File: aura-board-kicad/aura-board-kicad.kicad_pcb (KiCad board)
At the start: 2 copper layers, 76.8 x 53.3 mm, 22 parts, among them J1 Main Power, J2 PWM Outputs, J3 BB-UART0, J4 Attopilot, J5 GPS, J6 SBUS, J7 Telemetry, U1 TSR2-2450, U2 PocketBeagle, U3 Teensy-3.2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

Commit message: Add a proper 3x08 PWM block with ground pins and the power bus tied together but not connected to board power.
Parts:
- removed ? (x2): 1x08, Pin_Headers:Pin_Header_Straight_1x08_Pitch2.54mm
- J2: value PWM Outputs -> PWM; footprint Pin_Headers:Pin_Header_Straight_1x08_Pitch2.54mm -> footprint:PWM_3x08
- moved J2 17.8 mm to (92.1, 95.2), turned to 270 degrees
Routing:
- net +5VA: track 0.00 -> 17.8 mm

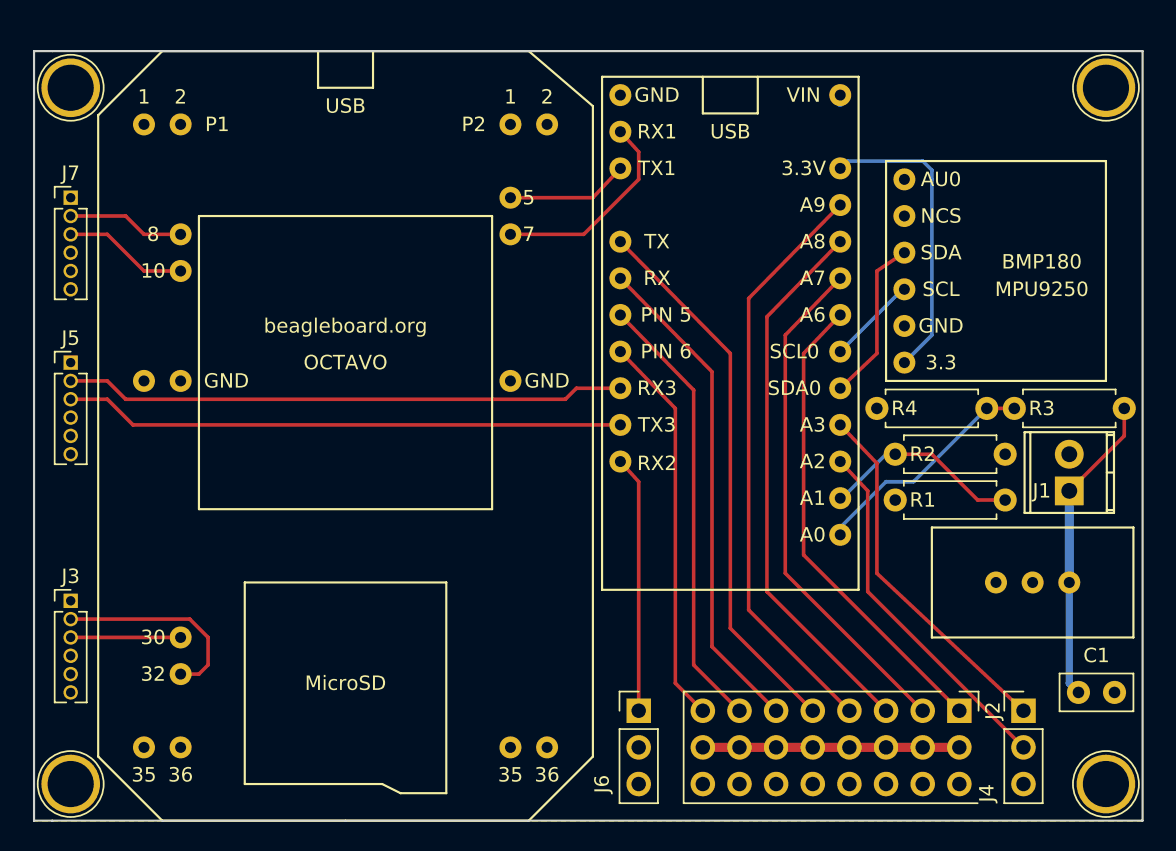
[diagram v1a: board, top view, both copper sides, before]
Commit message: Swich to picoblade 1.25mm external connectors.  DF-13 will also fit here. Pins 5 and 6 both tie to ground.  This means the assembler can pick 5 or 6 pos headers depending on their needs. This offers some flexibility to the assembler/integrator to pick the best suited connectors. Add external I2C0 connector (4-pin picoplade.)
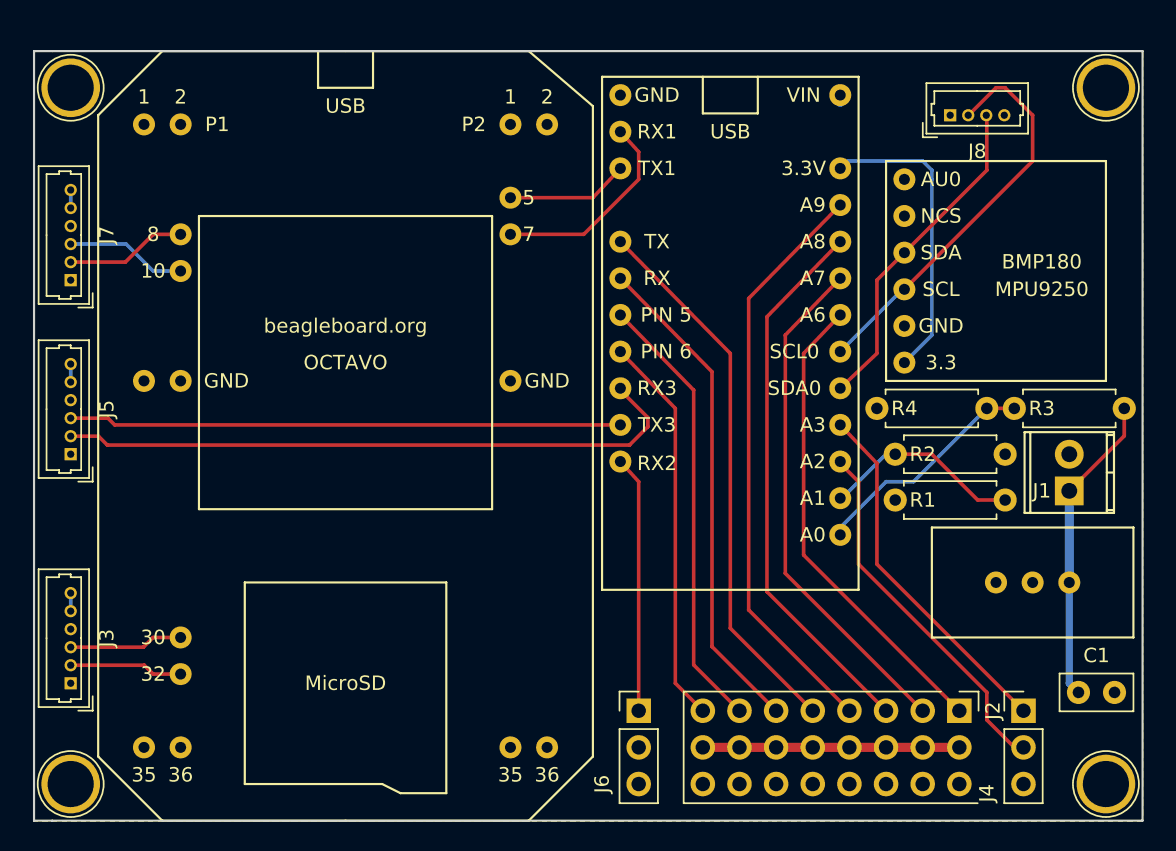
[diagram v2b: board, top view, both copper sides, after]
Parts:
- added J8: I2C0, Connectors_Molex:Molex_PicoBlade_53047-0410_04x1.25mm_Straight, F.Cu at (91.4, 54.0)
- J2: value PWM -> PWM_3x08
- J3: value BB-UART0 -> BB0; footprint Pin_Headers:Pin_Header_Straight_1x06_Pitch1.27mm -> Connectors_Molex:Molex_PicoBlade_53047-0610_06x1.25mm_Straight
- J5: footprint Pin_Headers:Pin_Header_Straight_1x06_Pitch1.27mm -> Connectors_Molex:Molex_PicoBlade_53047-0610_06x1.25mm_Straight
- J7: value Telemetry -> Tele; footprint Pin_Headers:Pin_Header_Straight_1x06_Pitch1.27mm -> Connectors_Molex:Molex_PicoBlade_53047-0610_06x1.25mm_Straight
- moved J5 6.35 mm to (30.5, 77.5), turned to 90 degrees
- moved J3 5.72 mm to (30.5, 93.3), turned to 90 degrees
- moved J7 5.72 mm to (30.5, 65.4), turned to 90 degrees
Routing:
- net /I2C0_SCL: track 6.23 -> 28.0 mm
- net /I2C0_SDA: track 11.5 -> 23.2 mm
- net /UART0_RX: track 14.1 -> 7.87 mm
- net /GPS_RX: track 38.9 -> 44.2 mm
- net GND: track 0.00 -> 3.75 mm
- net /GPS_TX: track 38.8 -> 38.3 mm
- net +5V: track 1.02 -> 0.51 mm

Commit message: Increase pad diameter (inner and outer) on all my project footprints to match standard 0.1" pin dimensions.
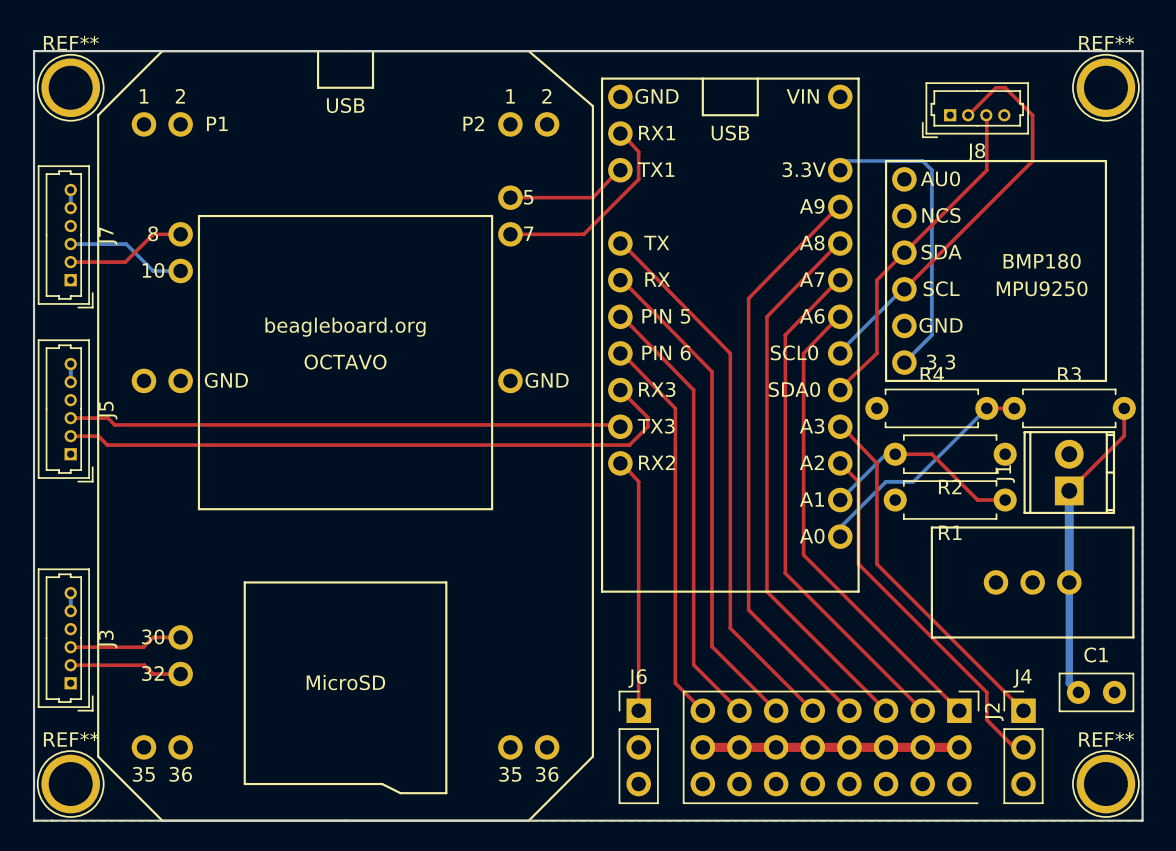
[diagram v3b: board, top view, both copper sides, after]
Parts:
- removed U1: TSR2-2450, Aura Footprints:TSR2-2450
- removed U2: PocketBeagle, Aura Footprints:PocketBeagle
- removed U3: Teensy-3.2, Aura Footprints:Teensy-3.2
- removed U4: CJMCU, Aura Footprints:CJMCU
- added THT: PocketBeagle, footprint:PocketBeagle, F.Cu at (49.5, 49.5)
- added THT: Teensy-3.2 (AuraUAS), footprint:Teensy-3.2, F.Cu at (76.2, 51.4)
- added THT: CJMCU, footprint:CJMCU, F.Cu at (94.6, 72.4)
- added THT: TSR2-2450, footprint:TSR2-2450, F.Cu at (97.2, 90.2)
- J3: value BB0 -> BBCON
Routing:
- net (no net): track 0.00 -> 50.5 mm
- net +3V3: track 20.9 -> 0.00 mm
- net /UART1_RX: track 14.3 -> 0.00 mm
- net /UART1_TX: track 8.50 -> 0.00 mm
- net /I2C0_SCL: track 28.0 -> 21.8 mm
- net +5V: track 0.51 -> 0.00 mm

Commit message: Clean up a small mess after trying to change pad size on all my custom footprints.
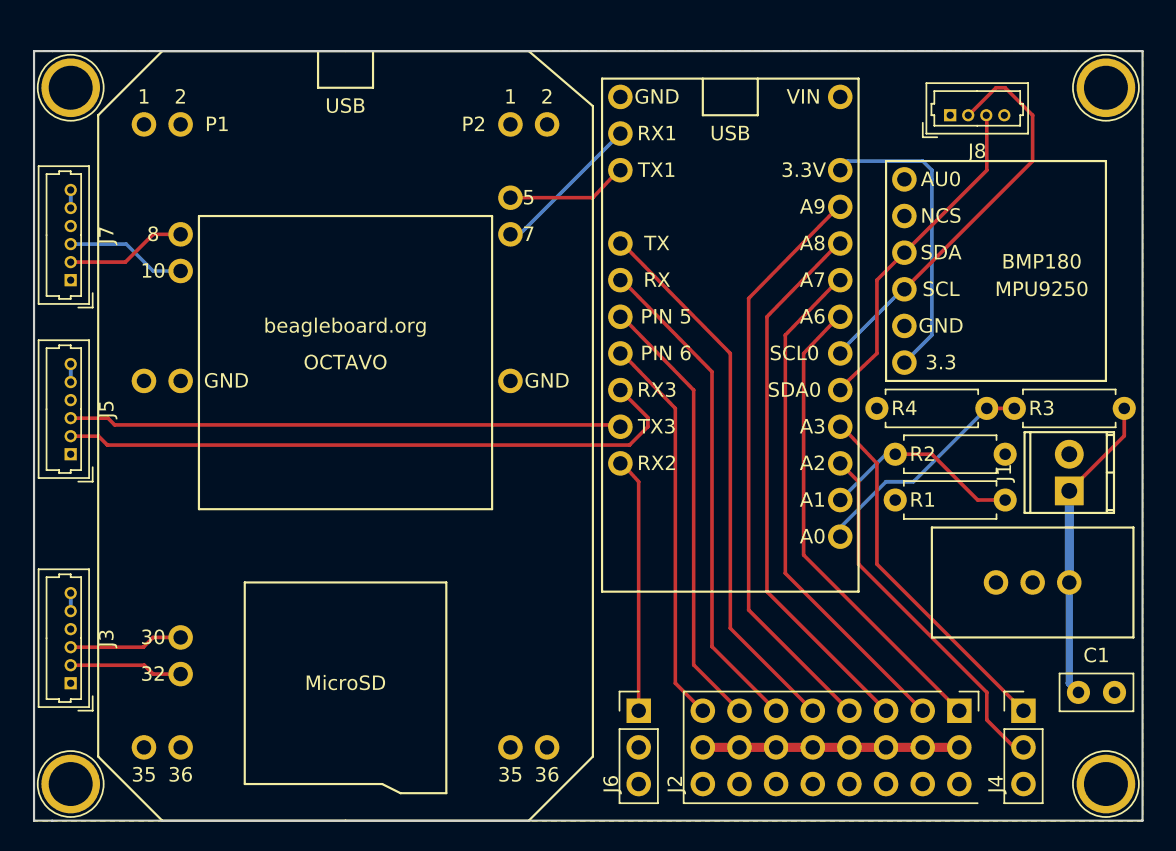
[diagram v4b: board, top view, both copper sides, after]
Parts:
- removed THT: PocketBeagle, footprint:PocketBeagle
- removed THT: Teensy-3.2 (AuraUAS), footprint:Teensy-3.2
- removed THT: CJMCU, footprint:CJMCU
- removed THT: TSR2-2450, footprint:TSR2-2450
- added U1: TSR2-2450, Aura Footprints:TSR2-2450, F.Cu at (97.2, 90.2)
- added U2: PocketBeagle, Aura Footprints:PocketBeagle, F.Cu at (49.5, 49.5)
- added U3: Teensy-3.2, Aura Footprints:Teensy-3.2, F.Cu at (76.2, 51.4)
- added U4: CJMCU, Aura Footprints:CJMCU, F.Cu at (94.6, 72.4)
- J4: value Attopilot -> Atto
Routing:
- net (no net): track 50.5 -> 0.00 mm
- net +3V3: track 0.00 -> 20.9 mm
- net /UART1_RX: track 0.00 -> 10.5 mm
- net /UART1_TX: track 0.00 -> 8.50 mm
- net /I2C0_SCL: track 21.8 -> 28.0 mm
- net +5V: track 0.00 -> 0.51 mm
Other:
- board text added: "+"
- board text added: "-"
- board text added: "1"
- board text added: "8"
- board text added: "S"
